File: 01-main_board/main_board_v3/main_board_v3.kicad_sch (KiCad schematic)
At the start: 12 parts, among them J1 FFC to Main_Peripheral, J2 FFC Analog, J3 FFC Digital

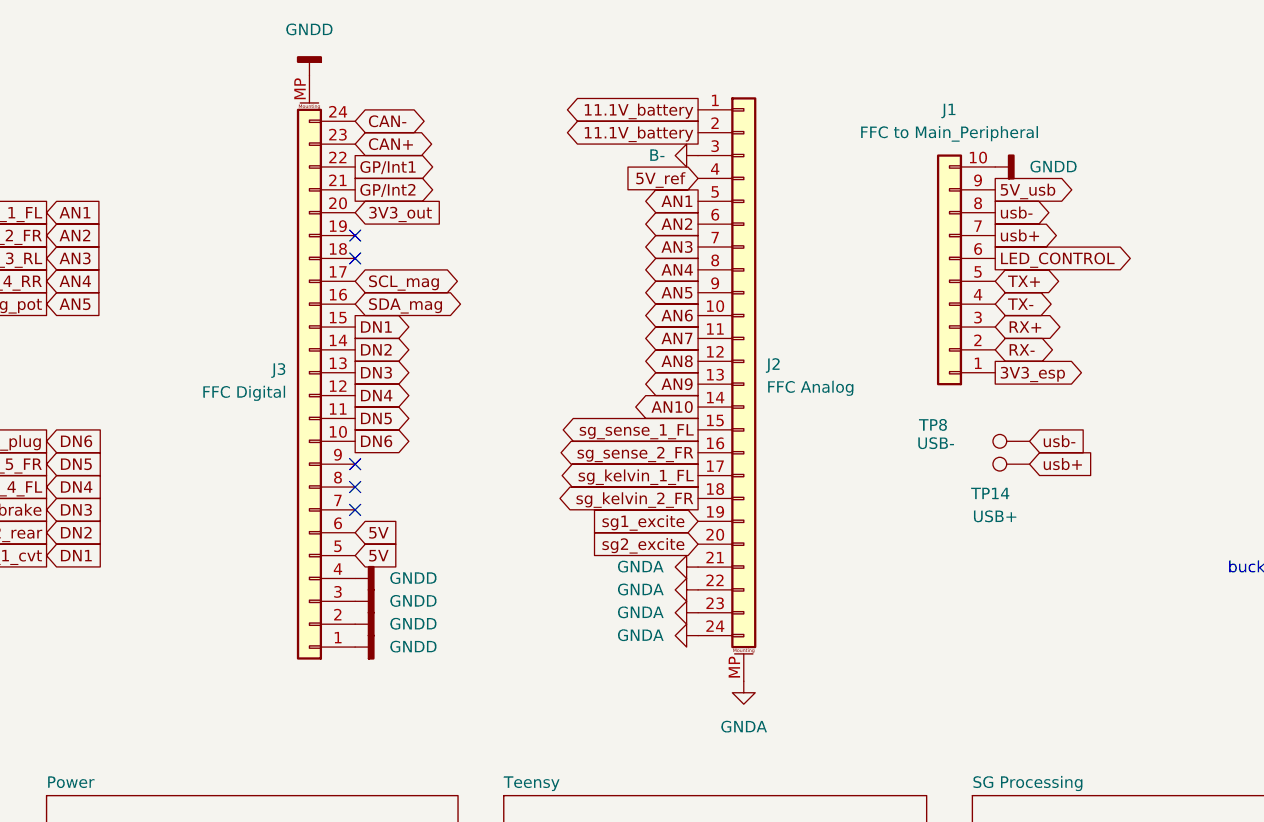
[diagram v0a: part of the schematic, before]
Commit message: arranged layout fully, traces almost done, planes wip
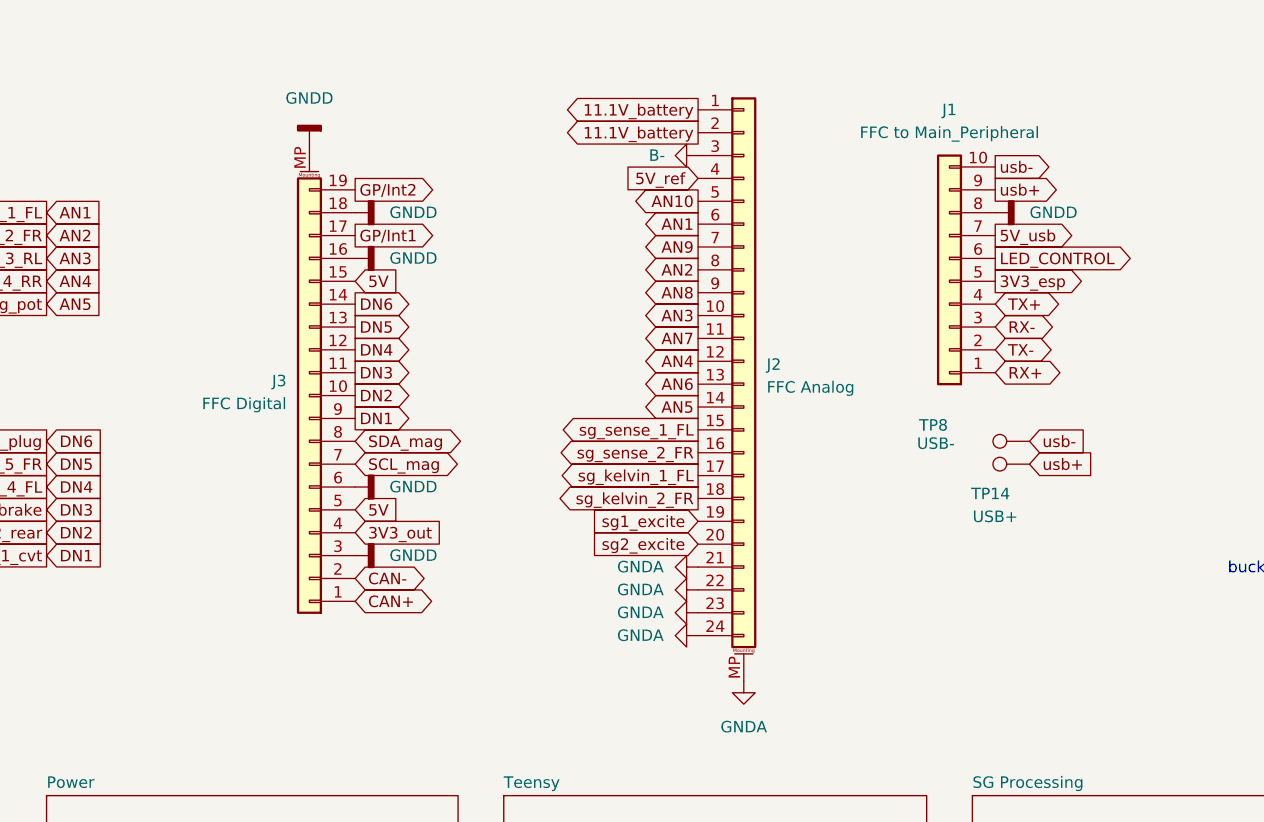
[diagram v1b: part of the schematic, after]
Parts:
- J1: footprint Connector_FFC-FPC:Molex_54548-1071_1x10-1MP_P0.5mm_Horizontal -> Connector_FFC-FPC:TE_1-84982-0_2Rows-10Pins-P1.0mm_Vertical
- J2: footprint (none) -> Connector_FFC-FPC:TE_2-84982-4_2Rows-24Pins-P1.0mm_Vertical
- J3: footprint (none) -> Connector_FFC-FPC:TE_1-84982-9_2Rows-19Pins-P1.0mm_Vertical; symbol Connector_Generic_MountingPin:Conn_01x24_MountingPin -> Connector_Generic_MountingPin:Conn_01x19_MountingPin
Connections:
- net 3V3_esp: now also J1.5 (Pin_5); no longer J1.1 (Pin_1)
- net 3V3_out: now also J3.4 (Pin_4); no longer J3.20 (Pin_20)
- net 5V: now also J3.15 (Pin_15); no longer J3.6 (Pin_6)
- net 5V_usb: now also J1.7 (Pin_7); no longer J1.9 (Pin_9)
- net AN1: now also J2.6 (Pin_6); no longer J2.5 (Pin_5)
- net AN10: now also J2.5 (Pin_5); no longer J2.14 (Pin_14)
- net AN2: now also J2.8 (Pin_8); no longer J2.6 (Pin_6)
- net AN3: now also J2.10 (Pin_10); no longer J2.7 (Pin_7)
- net AN4: now also J2.12 (Pin_12); no longer J2.8 (Pin_8)
- net AN5: now also J2.14 (Pin_14); no longer J2.9 (Pin_9)
- net AN6: now also J2.13 (Pin_13); no longer J2.10 (Pin_10)
- net AN8: now also J2.9 (Pin_9); no longer J2.12 (Pin_12)
- net AN9: now also J2.7 (Pin_7); no longer J2.13 (Pin_13)
- net CAN+: now also J3.1 (Pin_1); no longer J3.23 (Pin_23)
- net CAN-: now also J3.2 (Pin_2); no longer J3.24 (Pin_24)
- net DN1: now also J3.9 (Pin_9); no longer J3.15 (Pin_15)
- net DN2: now also J3.10 (Pin_10); no longer J3.14 (Pin_14)
- net DN3: now also J3.11 (Pin_11); no longer J3.13 (Pin_13)
- net DN5: now also J3.13 (Pin_13); no longer J3.11 (Pin_11)
- net DN6: now also J3.14 (Pin_14); no longer J3.10 (Pin_10)
- net GNDD: now also J1.8 (Pin_8), J3.16 (Pin_16), J3.18 (Pin_18), J3.6 (Pin_6); no longer J1.10 (Pin_10), J3.1 (Pin_1), J3.2 (Pin_2), J3.4 (Pin_4)
- net GP/Int1: now also J3.17 (Pin_17); no longer J3.22 (Pin_22)
- net GP/Int2: now also J3.19 (Pin_19); no longer J3.21 (Pin_21)
- net RX+: now also J1.1 (Pin_1); no longer J1.3 (Pin_3)
- net RX-: now also J1.3 (Pin_3); no longer J1.2 (Pin_2)
- net SCL_mag: now also J3.7 (Pin_7); no longer J3.17 (Pin_17)
- net SDA_mag: now also J3.8 (Pin_8); no longer J3.16 (Pin_16)
- net TX+: now also J1.4 (Pin_4); no longer J1.5 (Pin_5)
- net TX-: now also J1.2 (Pin_2); no longer J1.4 (Pin_4)
- net usb+: now also J1.9 (Pin_9); no longer J1.7 (Pin_7)
- net usb-: now also J1.10 (Pin_10); no longer J1.8 (Pin_8)
- no-connect marks 5 -> 0

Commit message: finished layout
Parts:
- H1, H2, H3, H4: footprint MountingHole:MountingHole_3.2mm_M3_Pad -> MountingHole:MountingHole_2.5mm_Pad
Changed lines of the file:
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@@
 			)
 		)
-		(property "Footprint" "MountingHole:MountingHole_3.2mm_M3_Pad"
+		(property "Footprint" "MountingHole:MountingHole_2.5mm_Pad"
 			(at 227.33 127 0)
 			(effects
@@
 			)
 		)
-		(property "Footprint" "MountingHole:MountingHole_3.2mm_M3_Pad"
+		(property "Footprint" "MountingHole:MountingHole_2.5mm_Pad"
 			(at 227.33 149.86 0)
 			(effects
@@
 			)
 		)
-		(property "Footprint" "MountingHole:MountingHole_3.2mm_M3_Pad"
+		(property "Footprint" "MountingHole:MountingHole_2.5mm_Pad"
 			(at 227.33 134.62 0)
 			(effects
@@
 			)
 		)
-		(property "Footprint" "MountingHole:MountingHole_3.2mm_M3_Pad"
+		(property "Footprint" "MountingHole:MountingHole_2.5mm_Pad"
 			(at 227.33 142.24 0)
 			(effects

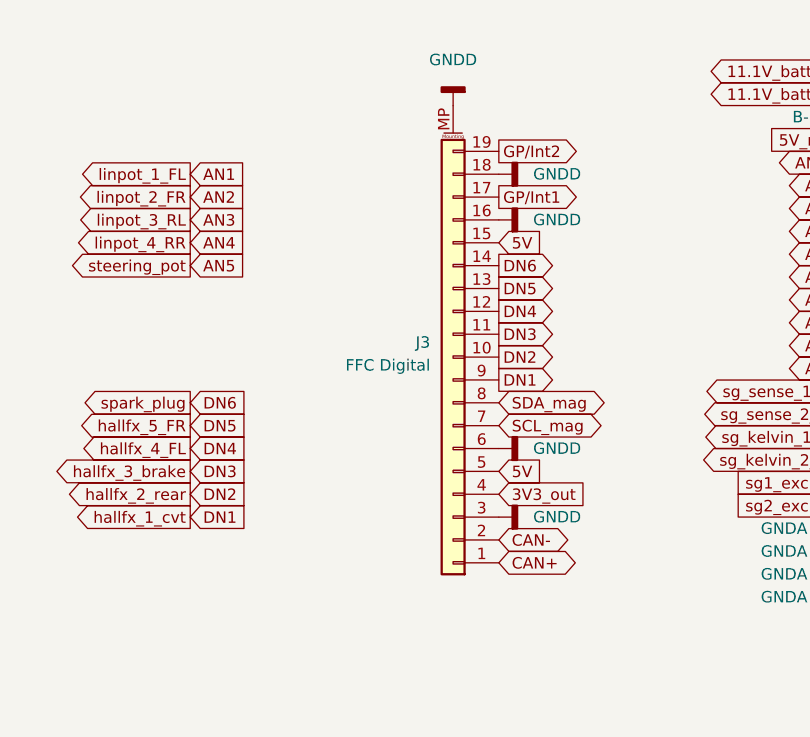
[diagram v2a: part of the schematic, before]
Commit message: added high speed signal gnd plane, updated fpc connectors
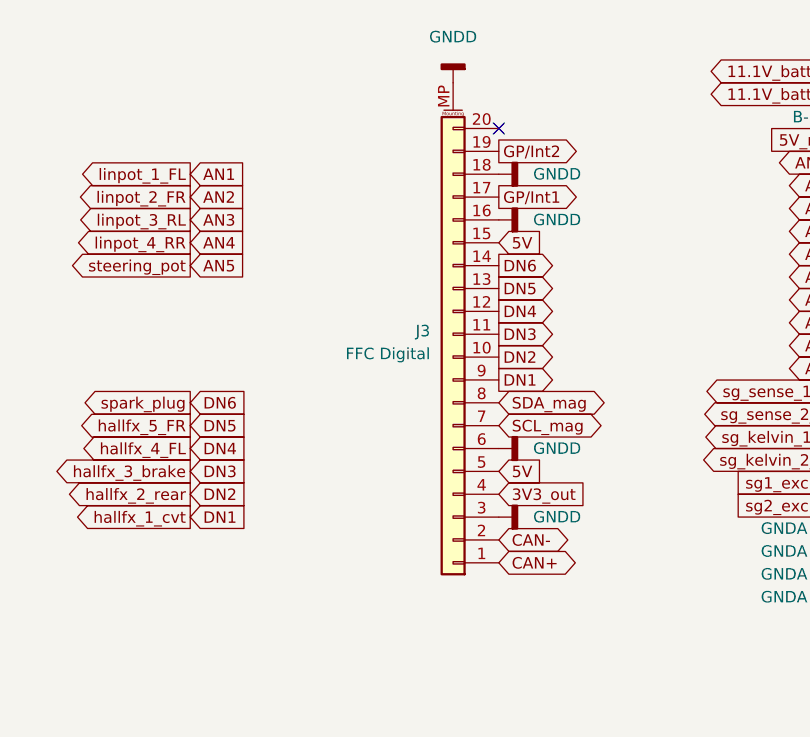
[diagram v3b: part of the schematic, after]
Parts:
- J3: footprint Connector_FFC-FPC:TE_1-84982-9_2Rows-19Pins-P1.0mm_Vertical -> Connector_FFC-FPC:TE_2-84982-0_2Rows-20Pins-P1.0mm_Vertical; symbol Connector_Generic_MountingPin:Conn_01x19_MountingPin -> Connector_Generic_MountingPin:Conn_01x20_MountingPin
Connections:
- no-connect marks 0 -> 1
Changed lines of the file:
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@@
 		)
 	)
+	(no_connect
+		(at 71.12 34.29)
+	)
 	(global_label "linpot_1_FL"
 		(shape output)
@@
 	)
 	(symbol
+		(lib_id "power:GNDD")
+		(at 66.04 29.21 180)
+		(unit 1)
+		(exclude_from_sim no)
+		(in_bom yes)
+		(on_board yes)
+		(dnp no)
+		(fields_autoplaced yes)
+		(property "Reference" "#PWR033"
+			(at 66.04 22.86 0)
+			(effects
+				(font
+					(size 1.27 1.27)
+				)
+				(hide yes)
+			)
+		)
+		(property "Value" "GNDD"
+			(at 66.04 24.13 0)
+			(effects
+				(font
+					(size 1.27 1.27)
+				)
+			)
+		)
+		(property "Footprint" ""
+			(at 66.04 29.21 0)
+			(effects
+				(font
+					(size 1.27 1.27)
+				)
+				(hide yes)
+			)
+		)
+		(property "Datasheet" ""
+			(at 66.04 29.21 0)
+			(effects
+				(font
+					(size 1.27 1.27)
+				)
+				(hide yes)
+			)
+		)
+		(property "Description" "Power symbol creates a global label with name \"GNDD\" , digital ground"
+			(at 66.04 29.21 0)
+			(effects
+				(font
+					(size 1.27 1.27)
+				)
+				(hide yes)
+			)
+		)
+		(pin "1"
+		)
+		(instances
+			(project "main_board_v3"
+				(path "/12c2237c-5932-49af-9119-92b28c846ae7"
+					(reference "#PWR033")
+					(unit 1)
+				)
+			)
+		)
+	)
+	(symbol
 		(lib_id "Connector:TestPoint")
 		(at 146.05 67.31 90)
@@
 	)
 	(symbol
-		(lib_id "power:GNDD")
-		(at 66.04 31.75 180)
-		(unit 1)
-		(exclude_from_sim no)
-		(in_bom yes)
-		(on_board yes)
-		(dnp no)
-		(fields_autoplaced yes)
-		(property "Reference" "#PWR033"
-			(at 66.04 25.4 0)
-			(effects
-				(font
-					(size 1.27 1.27)
-				)
-				(hide yes)
-			)
-		)
-		(property "Value" "GNDD"
-			(at 66.04 26.67 0)
-			(effects
-				(font
-					(size 1.27 1.27)
-				)
-			)
-		)
-		(property "Footprint" ""
-			(at 66.04 31.75 0)
-			(effects
-				(font
-					(size 1.27 1.27)
-				)
-				(hide yes)
-			)
-		)
-		(property "Datasheet" ""
-			(at 66.04 31.75 0)
-			(effects
-				(font
-					(size 1.27 1.27)
-				)
-				(hide yes)
-			)
-		)
-		(property "Description" "Power symbol creates a global label with name \"GNDD\" , digital ground"
-			(at 66.04 31.75 0)
-			(effects
-				(font
-					(size 1.27 1.27)
-				)
-				(hide yes)
-			)
-		)
-		(pin "1"
-		)
-		(instances
-			(project "main_board_v3"
-				(path "/12c2237c-5932-49af-9119-92b28c846ae7"
-					(reference "#PWR033")
-					(unit 1)
-				)
-			)
-		)
-	)
-	(symbol
 		(lib_id "Mechanical:MountingHole")
 		(at 227.33 127 0)
@@
 	)
 	(symbol
-		(lib_id "Connector_Generic_MountingPin:Conn_01x19_MountingPin")
+		(lib_id "Connector_Generic_MountingPin:Conn_01x20_MountingPin")
 		(at 66.04 59.69 180)
 		(unit 1)
@@
 		(fields_autoplaced yes)
 		(property "Reference" "J3"
-			(at 63.5 58.0643 0)
+			(at 63.5 56.7943 0)
 			(effects
 				(font
@@
 		)
 		(property "Value" "FFC Digital"
-			(at 63.5 60.6043 0)
+			(at 63.5 59.3343 0)
 			(effects
 				(font
@@
 			)
 		)
-		(property "Footprint" "Connector_FFC-FPC:TE_1-84982-9_2Rows-19Pins-P1.0mm_Vertical"
+		(property "Footprint" "Connector_FFC-FPC:TE_2-84982-0_2Rows-20Pins-P1.0mm_Vertical"
 			(at 66.04 59.69 0)
 			(effects
@@
 			)
 		)
-		(property "Description" "Generic connectable mounting pin connector, single row, 01x19, script generated (kicad-library-utils/schlib/autogen/connector/)"
+		(property "Description" "Generic connectable mounting pin connector, single row, 01x20, script generated (kicad-library-utils/schlib/autogen/connector/)"
 			(at 66.04 59.69 0)
 			(effects
@@
 		(pin "MP"
 		)
+		(pin "20"
+		)
 		(instances

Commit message: changed fpc connector footprint, which messed up spacing so have to redo a lot of layout
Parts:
- J1: footprint Connector_FFC-FPC:TE_1-84982-0_2Rows-10Pins-P1.0mm_Vertical -> Connector_FFC-FPC:TE_1-84952-0_1x10-1MP_P1.0mm_Horizontal
- J2: footprint Connector_FFC-FPC:TE_2-84982-4_2Rows-24Pins-P1.0mm_Vertical -> Connector_FFC-FPC:TE_2-84952-4_1x24-1MP_P1.0mm_Horizontal
- J3: footprint Connector_FFC-FPC:TE_2-84982-0_2Rows-20Pins-P1.0mm_Vertical -> Connector_FFC-FPC:TE_2-84952-0_1x20-1MP_P1.0mm_Horizontal
- TP14, TP8: footprint TestPoint:TestPoint_Pad_1.0x1.0mm -> TestPoint:TestPoint_Pad_D1.0mm
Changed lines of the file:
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@@
 			)
 		)
-		(property "Footprint" "Connector_FFC-FPC:TE_1-84982-0_2Rows-10Pins-P1.0mm_Vertical"
+		(property "Footprint" "Connector_FFC-FPC:TE_1-84952-0_1x10-1MP_P1.0mm_Horizontal"
 			(at 137.16 46.99 0)
 			(effects
@@
 			)
 		)
-		(property "Footprint" "TestPoint:TestPoint_Pad_1.0x1.0mm"
+		(property "Footprint" "TestPoint:TestPoint_Pad_D1.0mm"
 			(at 146.05 62.23 0)
 			(effects
@@
 			)
 		)
-		(property "Footprint" "Connector_FFC-FPC:TE_2-84982-4_2Rows-24Pins-P1.0mm_Vertical"
+		(property "Footprint" "Connector_FFC-FPC:TE_2-84952-4_1x24-1MP_P1.0mm_Horizontal"
 			(at 114.3 55.88 0)
 			(effects
@@
 			)
 		)
-		(property "Footprint" "Connector_FFC-FPC:TE_2-84982-0_2Rows-20Pins-P1.0mm_Vertical"
+		(property "Footprint" "Connector_FFC-FPC:TE_2-84952-0_1x20-1MP_P1.0mm_Horizontal"
 			(at 66.04 59.69 0)
 			(effects
@@
 			)
 		)
-		(property "Footprint" "TestPoint:TestPoint_Pad_1.0x1.0mm"
+		(property "Footprint" "TestPoint:TestPoint_Pad_D1.0mm"
 			(at 146.05 59.69 0)
 			(effects

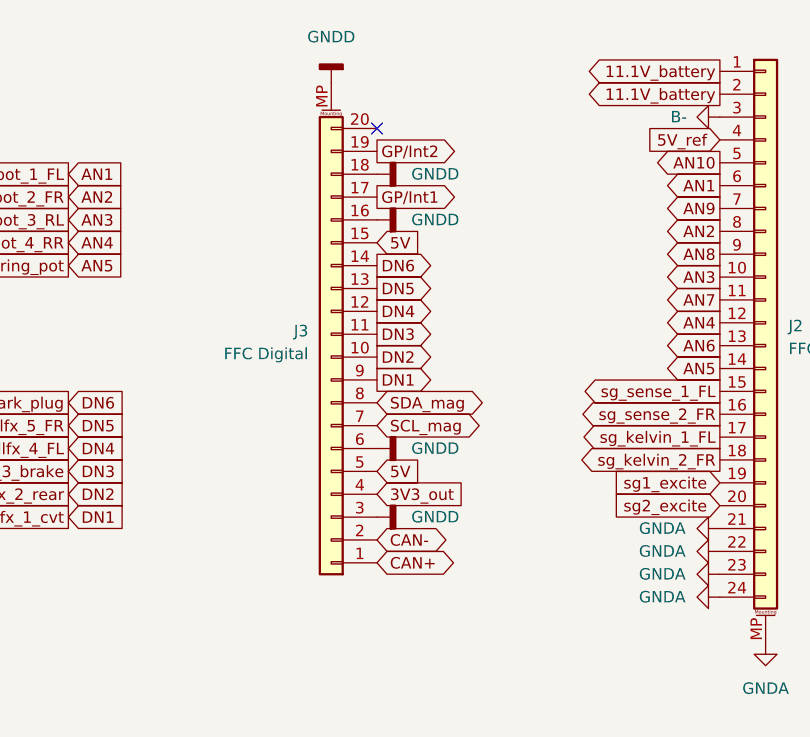
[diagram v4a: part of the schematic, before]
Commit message: fixed board to use horizontal fpc connectors, length matched all diff pairs + cleaned up layout
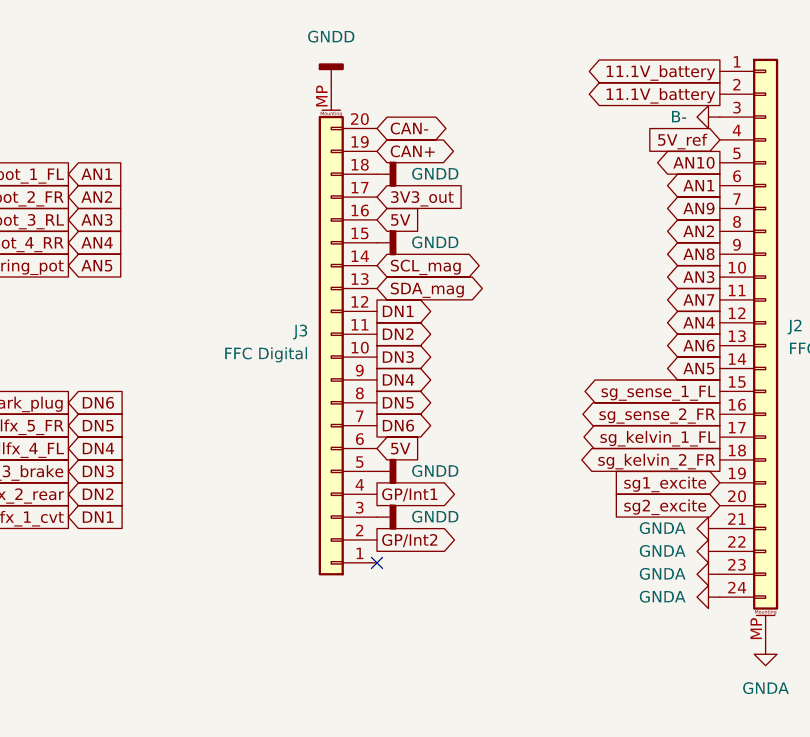
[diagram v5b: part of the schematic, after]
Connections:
- net 3V3_out: now also J3.17 (Pin_17); no longer J3.4 (Pin_4)
- net 5V: now also J3.16 (Pin_16), J3.6 (Pin_6); no longer J3.15 (Pin_15), J3.5 (Pin_5)
- net CAN+: now also J3.19 (Pin_19); no longer J3.1 (Pin_1)
- net CAN-: now also J3.20 (Pin_20); no longer J3.2 (Pin_2)
- net DN1: now also J3.12 (Pin_12); no longer J3.9 (Pin_9)
- net DN2: now also J3.11 (Pin_11); no longer J3.10 (Pin_10)
- net DN3: now also J3.10 (Pin_10); no longer J3.11 (Pin_11)
- net DN4: now also J3.9 (Pin_9); no longer J3.12 (Pin_12)
- net DN5: now also J3.8 (Pin_8); no longer J3.13 (Pin_13)
- net DN6: now also J3.7 (Pin_7); no longer J3.14 (Pin_14)
- net GNDD: now also J3.15 (Pin_15), J3.5 (Pin_5); no longer J3.16 (Pin_16), J3.6 (Pin_6)
- net GP/Int1: now also J3.4 (Pin_4); no longer J3.17 (Pin_17)
- net GP/Int2: now also J3.2 (Pin_2); no longer J3.19 (Pin_19)
- net SCL_mag: now also J3.14 (Pin_14); no longer J3.7 (Pin_7)
- net SDA_mag: now also J3.13 (Pin_13); no longer J3.8 (Pin_8)
